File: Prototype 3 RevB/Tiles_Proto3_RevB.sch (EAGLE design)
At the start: 62 parts, among them Q1 DMG3415U-7, U2 MF-DSC-SOT233-MMBT3904, X1 32.768

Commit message: finished placing proto3revB
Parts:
- removed C12: 0.1uF, microbuilder2:CAP_CERAMIC0603_NO
- added C8: (no value), MF_Passives:CAPACITOR_NP_0603
- B+, B-: device wirepad:1,6/0,8 -> wirepad:SMD2
- C1: value 1uF -> (none)
- C10: value 10µF -> (none); device microbuilder2:CAP_CERAMIC0805-NOOUTLINE -> MF_Passives:CAPACITOR_NP_0805
- C11: value 10µF -> (none); device microbuilder2:CAP_CERAMIC0805-NOOUTLINE -> MF_Passives:CAPACITOR_NP_0603
- C2: value 100nf -> (none); device Seeed-OPL-Capacitor:CERAMIC-100NF-50V-10%-X7R(0603) -> MF_Passives:CAPACITOR_NP_0603
- C3: value 10uF -> (none)
- C4: value 22pF -> (none)
- C5: value 10uf -> (none); device Seeed-OPL-Capacitor:CERAMIC-10UF-10V-10%-X5R(0603) -> MF_Passives:CAPACITOR_NP_0603
- C6, C7: value 1uf -> (none); device Seeed-OPL-Capacitor:CERAMIC-1UF-25V-10%-X7R(0603) -> MF_Passives:CAPACITOR_NP_0603
- C9: value 22pF -> (none); device MF_Passives:CAPACITOR_NP_0603 -> MF_Passives:CAPACITOR_NP_0805
- J1: device tiles:CONN_07_SIMSQPAD_BOTTOM -> SparkFun-Connectors:CONN_07
- R1, R2, R3, R4, R7: value 10K 1/10W -> (none); device Seeed-OPL-Resistor:SMD-RES-10K-5%-1/10W(0603) -> MF_Passives:RESISTOR_0603
- R10, R9: value 100K -> (none); device microbuilder2:RESISTOR_0603_NOOUT -> MF_Passives:RESISTOR_0603
- R11: value 10K -> (none); device microbuilder2:RESISTOR_0603_NOOUT -> MF_Passives:RESISTOR_0603
- R12, R13, R14, R15, R6: value 330 -> (none)
- R5: value 100K 1/10W -> (none); device Seeed-OPL-Resistor:SMD-RES-100K-5%-1/10W(0603) -> MF_Passives:RESISTOR_0603
- R8: value 1K 1/10W -> (none); device Seeed-OPL-Resistor:SMD-RES-10K-5%-1/10W(0603) -> MF_Passives:RESISTOR_0603
- TP2, TP3, TP4, TP5, TP6: device microbuilder2:TESTPOINT1.5X2.0MM_NOCREAM -> microbuilder2:TESTPOINTROUND2MM
- renumbered STAT1 to BTL
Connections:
- net 3.3V: now also C2.P$1, C5.P$1, C7.P$1, C9.P$1, R1.P$1, R11.P$2, R2.P$1, R3.P$1, R8.P$1; no longer C10.1, C2.1, C5.1, C7.2, R1.1, R11.1, R2.2, R3.2, R8.2
- net BUZZER: now also R7.P$2; no longer R7.2
- net CAP-INT: now also R3.P$2; no longer R3.1
- net CAP-RES: now also R4.P$1; no longer R4.2
- net DTR: now also C11.P$1; no longer C12.1
- net GND: now also C10.P$2, C2.P$2, C5.P$2, C6.P$2, C7.P$2, C8.P$2, R4.P$2, R5.P$2, R7.P$1, R9.P$2; no longer C10.2, C11.2, C2.2, C5.2, C6.1, C7.1, R4.1, R5.1, R7.1, R9.2
- net N$10: now also R10.P$2; no longer R10.2
- net N$12: now also C8.P$1; no longer C9.P$1
- net N$13: now also C10.P$1, R10.P$1; no longer C11.1, R10.1
- net N$20: now also C11.P$2; no longer C12.2
- net N$3: now also R5.P$1; no longer R5.2
- net N$4: now also R8.P$2; no longer R8.1
- net N$5: now also C6.P$1; no longer C6.2
- net RESET: now also R11.P$1; no longer R11.2
- net SCL: now also R1.P$2; no longer R1.2
- net SDA: now also R2.P$2; no longer R2.1
- net VBUS: now also R9.P$1; no longer R9.1
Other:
- moved on the sheet: C9

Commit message: partial routing
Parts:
- renumbered TP1 to FRST, TP2 to SWDIO, TP3 to SWCLK, TP4 to RST, TP5 to DFU, TP6 to SWO
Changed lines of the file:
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@@
 <part name="U$7" library="microbuilder" deviceset="GND" device=""/>
 <part name="U$8" library="microbuilder" deviceset="GND" device=""/>
-<part name="TP1" library="microbuilder2" deviceset="TESTPOINT" device="1.5X2.0MM_NOCREAM"/>
-<part name="TP2" library="microbuilder2" deviceset="TESTPOINT" device="ROUND2MM"/>
-<part name="TP3" library="microbuilder2" deviceset="TESTPOINT" device="ROUND2MM"/>
-<part name="TP4" library="microbuilder2" deviceset="TESTPOINT" device="ROUND2MM"/>
-<part name="TP5" library="microbuilder2" deviceset="TESTPOINT" device="ROUND2MM"/>
-<part name="TP6" library="microbuilder2" deviceset="TESTPOINT" device="ROUND2MM"/>
+<part name="FRST" library="microbuilder2" deviceset="TESTPOINT" device="1.5X2.0MM_NOCREAM"/>
+<part name="SWDIO" library="microbuilder2" deviceset="TESTPOINT" device="ROUND2MM"/>
+<part name="SWCLK" library="microbuilder2" deviceset="TESTPOINT" device="ROUND2MM"/>
+<part name="RST" library="microbuilder2" deviceset="TESTPOINT" device="ROUND2MM"/>
+<part name="DFU" library="microbuilder2" deviceset="TESTPOINT" device="ROUND2MM"/>
+<part name="SWO" library="microbuilder2" deviceset="TESTPOINT" device="ROUND2MM"/>
 <part name="U$10" library="microbuilder2" deviceset="3.3V" device=""/>
 <part name="U$11" library="microbuilder2" deviceset="VBAT" device=""/>
@@
 <instance part="U$7" gate="G$1" x="-2.54" y="68.58"/>
 <instance part="U$8" gate="G$1" x="60.96" y="78.74" rot="R180"/>
-<instance part="TP1" gate="G$1" x="60.96" y="68.58" rot="R270"/>
-<instance part="TP2" gate="G$1" x="60.96" y="66.04" rot="R270"/>
-<instance part="TP3" gate="G$1" x="60.96" y="63.5" rot="R270"/>
-<instance part="TP4" gate="G$1" x="60.96" y="60.96" rot="R270"/>
-<instance part="TP5" gate="G$1" x="60.96" y="58.42" rot="R270"/>
-<instance part="TP6" gate="G$1" x="60.96" y="53.34" rot="R270"/>
+<instance part="FRST" gate="G$1" x="60.96" y="68.58" rot="R270"/>
+<instance part="SWDIO" gate="G$1" x="60.96" y="66.04" rot="R270"/>
+<instance part="SWCLK" gate="G$1" x="60.96" y="63.5" rot="R270"/>
+<instance part="RST" gate="G$1" x="60.96" y="60.96" rot="R270"/>
+<instance part="DFU" gate="G$1" x="60.96" y="58.42" rot="R270"/>
+<instance part="SWO" gate="G$1" x="60.96" y="53.34" rot="R270"/>
 <instance part="U$10" gate="G$1" x="43.18" y="162.56"/>
 <instance part="U$11" gate="G$1" x="2.54" y="162.56"/>
@@
 <segment>
 <pinref part="U1" gate="G$1" pin="P0.21/RESET"/>
-<pinref part="TP4" gate="G$1" pin="P$1"/>
+<pinref part="RST" gate="G$1" pin="P$1"/>
 <wire x1="45.72" y1="60.96" x2="60.96" y2="60.96" width="0.1524" layer="91"/>
 <label x="48.26" y="60.96" size="1.778" layer="95"/>
@@
 <segment>
 <pinref part="U1" gate="G$1" pin="P0.22"/>
-<pinref part="TP1" gate="G$1" pin="P$1"/>
+<pinref part="FRST" gate="G$1" pin="P$1"/>
 <wire x1="45.72" y1="68.58" x2="60.96" y2="68.58" width="0.1524" layer="91"/>
 <label x="48.26" y="68.58" size="1.778" layer="95"/>
@@
 <segment>
 <pinref part="U1" gate="G$1" pin="SWDIO"/>
-<pinref part="TP2" gate="G$1" pin="P$1"/>
+<pinref part="SWDIO" gate="G$1" pin="P$1"/>
 <wire x1="45.72" y1="66.04" x2="60.96" y2="66.04" width="0.1524" layer="91"/>
 <label x="48.26" y="66.04" size="1.778" layer="95"/>
@@
 <segment>
 <pinref part="U1" gate="G$1" pin="SWDCLK"/>
-<pinref part="TP3" gate="G$1" pin="P$1"/>
+<pinref part="SWCLK" gate="G$1" pin="P$1"/>
 <wire x1="45.72" y1="63.5" x2="60.96" y2="63.5" width="0.1524" layer="91"/>
 <label x="48.26" y="63.5" size="1.778" layer="95"/>
@@
 <segment>
 <pinref part="U1" gate="G$1" pin="P0.20"/>
-<pinref part="TP5" gate="G$1" pin="P$1"/>
+<pinref part="DFU" gate="G$1" pin="P$1"/>
 <wire x1="45.72" y1="58.42" x2="60.96" y2="58.42" width="0.1524" layer="91"/>
 <label x="48.26" y="58.42" size="1.778" layer="95"/>
@@
 <segment>
 <pinref part="U1" gate="G$1" pin="P0.18/SWO"/>
-<pinref part="TP6" gate="G$1" pin="P$1"/>
+<pinref part="SWO" gate="G$1" pin="P$1"/>
 <wire x1="45.72" y1="53.34" x2="60.96" y2="53.34" width="0.1524" layer="91"/>
 <label x="48.26" y="53.34" size="1.778" layer="95"/>

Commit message: ready for prod
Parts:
- removed IMU: ADXL345BCCZ-RL, Seeed-OPL-sensor:MOTION/POSITION-ADXL345BCCZ-RL(14P-5.0X3.0MM)
- added EN: (no value), SparkFun-Connectors:CONN_021X02_NO_SILK
- added T2: MF-DSC-SOT233-MMBT3904, MF_Discrete_Semiconductor:NPN_BJTMMBT3904_SOT-23-3
- U1: value (none) -> MDBT42Q
- U2: value MF-DSC-SOT233-MMBT3904 -> AP2112; device MF_Discrete_Semiconductor:NPN_BJTMMBT3904_SOT-23-3 -> microbuilder2:VREG_SOT23-5
- U3: value (none) -> ADXL345; device microbuilder2:VREG_SOT23-5 -> Seeed-OPL-sensor:MOTION/POSITION-ADXL345BCCZ-RL(14P-5.0X3.0MM)
- U4: value (none) -> CAP1188
- renumbered CAP to U4, HAPTIC to U5
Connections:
- removed net N$10: R10.P$2, U3.EN
- new net EN: EN.1, R10.P$2, U2.EN
- net 3.3V: now also U2.OUT, U3.!CS, U3.VDDI/O, U3.VS; no longer IMU.!CS, IMU.VDDI/O, IMU.VS, U3.OUT
- net BUZZER: now also T2.BASE; no longer U2.BASE
- net GND: now also EN.2, T2.EMITTER, U2.GND, U3.GND@1, U3.GND@2, U3.GND@3; no longer IMU.GND@1, IMU.GND@2, IMU.GND@3, U2.EMITTER, U3.GND
- net IMU-INT: now also U3.INT1; no longer IMU.INT1
- net N$13: now also U2.IN; no longer U3.IN
- net N$4: now also T2.COLLECTOR; no longer U2.COLLECTOR
- net SCL: now also U3.SCL/SCLK; no longer IMU.SCL/SCLK
- net SDA: now also U3.SDA/SDI/SDIO; no longer IMU.SDA/SDI/SDIO

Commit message: values back in sch
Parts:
- C1, C6, C7: value (none) -> 1uF
- C10, C5, C9: value (none) -> 10uF
- C11: value (none) -> 0.1uF
- C2: value (none) -> 100nF
- C4, C8: value (none) -> 22pF
- L1: value (none) -> 10uH
- R1, R11, R2, R3, R4, R7: value (none) -> 10K
- R10, R5, R9: value (none) -> 100K
- R12: value (none) -> 27
- R13, R14: value (none) -> 22
- R15, R6: value (none) -> 330
- R8: value (none) -> 1K
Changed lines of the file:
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@@
 <part name="SW" library="MF_Switches" deviceset="TACT" device="_4.2MM" value="MF-SW-TACT-4.2MM"/>
 <part name="STAT" library="MF_LEDs" deviceset="LED_SINGLE" device="-0603-RED" value="MF-LED-0603-RED"/>
-<part name="R6" library="MF_Passives" deviceset="RESISTOR" device="_0603"/>
+<part name="R6" library="MF_Passives" deviceset="RESISTOR" device="_0603" value="330"/>
 <part name="U$21" library="microbuilder" deviceset="GND" device=""/>
 <part name="U$25" library="microbuilder" deviceset="GND" device=""/>
@@
 <part name="U3" library="Seeed-OPL-sensor" deviceset="MOTION/POSITION-ADXL345BCCZ-RL(14P-5.0X3.0MM)" device="" value="ADXL345"/>
 <part name="U1" library="microbuilder2" deviceset="NRF52832_MODULE_MDBT42" device="" value="MDBT42Q"/>
-<part name="C1" library="MF_Passives" deviceset="CAPACITOR_NP" device="_0603"/>
+<part name="C1" library="MF_Passives" deviceset="CAPACITOR_NP" device="_0603" value="1uF"/>
 <part name="C3" library="MF_Passives" deviceset="CAPACITOR_NP" device="_0603"/>
-<part name="C4" library="MF_Passives" deviceset="CAPACITOR_NP" device="_0603"/>
-<part name="C8" library="MF_Passives" deviceset="CAPACITOR_NP" device="_0603"/>
-<part name="L1" library="MF_Passives" deviceset="INDUCTOR" device="_0603"/>
+<part name="C4" library="MF_Passives" deviceset="CAPACITOR_NP" device="_0603" value="22pF"/>
+<part name="C8" library="MF_Passives" deviceset="CAPACITOR_NP" device="_0603" value="22pF"/>
+<part name="L1" library="MF_Passives" deviceset="INDUCTOR" device="_0603" value="10uH"/>
 <part name="U$1" library="microbuilder2" deviceset="3.3V" device=""/>
 <part name="U$2" library="microbuilder" deviceset="GND" device=""/>
@@
 <part name="U$35" library="microbuilder" deviceset="GND" device=""/>
 <part name="P+2" library="microbuilder2" deviceset="3.3V" device=""/>
-<part name="R12" library="MF_Passives" deviceset="RESISTOR" device="_0603"/>
-<part name="R13" library="MF_Passives" deviceset="RESISTOR" device="_0603"/>
-<part name="R14" library="MF_Passives" deviceset="RESISTOR" device="_0603"/>
+<part name="R12" library="MF_Passives" deviceset="RESISTOR" device="_0603" value="27"/>
+<part name="R13" library="MF_Passives" deviceset="RESISTOR" device="_0603" value="22"/>
+<part name="R14" library="MF_Passives" deviceset="RESISTOR" device="_0603" value="22"/>
 <part name="D3" library="MF_LEDs" deviceset="LED_RGB_CA" device="_PLCC4" value="MF-LED-3228-RGB"/>
 <part name="BTL" library="MF_LEDs" deviceset="LED_SINGLE" device="-0603-RED" value="MF-LED-0603-RED"/>
-<part name="R15" library="MF_Passives" deviceset="RESISTOR" device="_0603"/>
+<part name="R15" library="MF_Passives" deviceset="RESISTOR" device="_0603" value="330"/>
 <part name="U$18" library="microbuilder" deviceset="GND" device=""/>
-<part name="R9" library="MF_Passives" deviceset="RESISTOR" device="_0603"/>
-<part name="R10" library="MF_Passives" deviceset="RESISTOR" device="_0603"/>
-<part name="R11" library="MF_Passives" deviceset="RESISTOR" device="_0603"/>
-<part name="R1" library="MF_Passives" deviceset="RESISTOR" device="_0603"/>
-<part name="R2" library="MF_Passives" deviceset="RESISTOR" device="_0603"/>
-<part name="R3" library="MF_Passives" deviceset="RESISTOR" device="_0603"/>
-<part name="R4" library="MF_Passives" deviceset="RESISTOR" device="_0603"/>
-<part name="R5" library="MF_Passives" deviceset="RESISTOR" device="_0603"/>
-<part name="R7" library="MF_Passives" deviceset="RESISTOR" device="_0603"/>
-<part name="R8" library="MF_Passives" deviceset="RESISTOR" device="_0603"/>
-<part name="C2" library="MF_Passives" deviceset="CAPACITOR_NP" device="_0603"/>
-<part name="C5" library="MF_Passives" deviceset="CAPACITOR_NP" device="_0603"/>
-<part name="C6" library="MF_Passives" deviceset="CAPACITOR_NP" device="_0603"/>
-<part name="C7" library="MF_Passives" deviceset="CAPACITOR_NP" device="_0603"/>
-<part name="C9" library="MF_Passives" deviceset="CAPACITOR_NP" device="_0805"/>
-<part name="C10" library="MF_Passives" deviceset="CAPACITOR_NP" device="_0805"/>
-<part name="C11" library="MF_Passives" deviceset="CAPACITOR_NP" device="_0603"/>
+<part name="R9" library="MF_Passives" deviceset="RESISTOR" device="_0603" value="100K"/>
+<part name="R10" library="MF_Passives" deviceset="RESISTOR" device="_0603" value="100K"/>
+<part name="R11" library="MF_Passives" deviceset="RESISTOR" device="_0603" value="10K"/>
+<part name="R1" library="MF_Passives" deviceset="RESISTOR" device="_0603" value="10K"/>
+<part name="R2" library="MF_Passives" deviceset="RESISTOR" device="_0603" value="10K"/>
+<part name="R3" library="MF_Passives" deviceset="RESISTOR" device="_0603" value="10K"/>
+<part name="R4" library="MF_Passives" deviceset="RESISTOR" device="_0603" value="10K"/>
+<part name="R5" library="MF_Passives" deviceset="RESISTOR" device="_0603" value="100K"/>
+<part name="R7" library="MF_Passives" deviceset="RESISTOR" device="_0603" value="10K"/>
+<part name="R8" library="MF_Passives" deviceset="RESISTOR" device="_0603" value="1K"/>
+<part name="C2" library="MF_Passives" deviceset="CAPACITOR_NP" device="_0603" value="100nF"/>
+<part name="C5" library="MF_Passives" deviceset="CAPACITOR_NP" device="_0603" value="10uF"/>
+<part name="C6" library="MF_Passives" deviceset="CAPACITOR_NP" device="_0603" value="1uF"/>
+<part name="C7" library="MF_Passives" deviceset="CAPACITOR_NP" device="_0603" value="1uF"/>
+<part name="C9" library="MF_Passives" deviceset="CAPACITOR_NP" device="_0805" value="10uF"/>
+<part name="C10" library="MF_Passives" deviceset="CAPACITOR_NP" device="_0805" value="10uF"/>
+<part name="C11" library="MF_Passives" deviceset="CAPACITOR_NP" device="_0603" value="0.1uF"/>
 <part name="B+" library="wirepad" deviceset="SMD2" device=""/>
 <part name="B-" library="wirepad" deviceset="SMD2" device=""/>

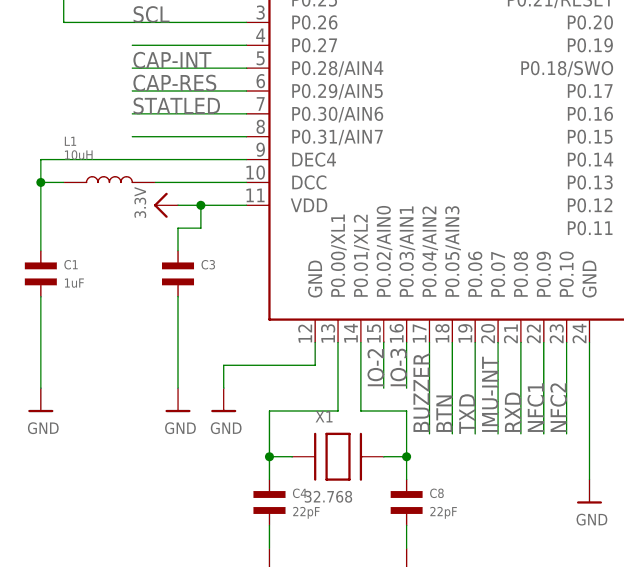
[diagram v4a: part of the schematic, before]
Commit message: re-added part values
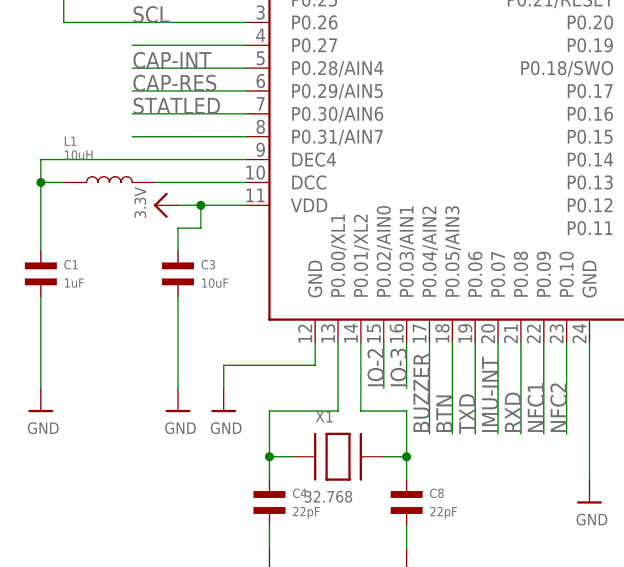
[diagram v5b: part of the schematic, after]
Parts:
- C3: value (none) -> 10uF
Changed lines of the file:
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@@
 <part name="U1" library="microbuilder2" deviceset="NRF52832_MODULE_MDBT42" device="" value="MDBT42Q"/>
 <part name="C1" library="MF_Passives" deviceset="CAPACITOR_NP" device="_0603" value="1uF"/>
-<part name="C3" library="MF_Passives" deviceset="CAPACITOR_NP" device="_0603"/>
+<part name="C3" library="MF_Passives" deviceset="CAPACITOR_NP" device="_0603" value="10uF"/>
 <part name="C4" library="MF_Passives" deviceset="CAPACITOR_NP" device="_0603" value="22pF"/>
 <part name="C8" library="MF_Passives" deviceset="CAPACITOR_NP" device="_0603" value="22pF"/>
@@
 </sheet>
 </sheets>
+<errors>
+</errors>
 </schematic>
 </drawing>

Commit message: ready for prod
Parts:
- BTL: value MF-LED-0603-RED -> RED
- BUZZER: HOUSEPART (none) -> no; MPN (none) -> 490-CMT-4023S-SMT-TR; POPULATE (none) -> 1
- C1, C6, C7: HOUSEPART (none) -> YES; MPN (none) -> MF-CAP-0603-1uF
- C10, C9: device MF_Passives:CAPACITOR_NP_0805 -> MF_Passives:CAPACITOR_NP_1206; HOUSEPART (none) -> YES; MPN (none) -> MF-CAP-1206-10uF
- C11: HOUSEPART (none) -> YES; MPN (none) -> MF-CAP-0603-0.1uF
- C2: value 100nF -> 0.1uF; HOUSEPART (none) -> YES; MPN (none) -> MF-CAP-0603-0.1uF
- C3, C5: device MF_Passives:CAPACITOR_NP_0603 -> MF_Passives:CAPACITOR_NP_1206; HOUSEPART (none) -> YES; MPN (none) -> MF-CAP-1206-10uF
- C4, C8: HOUSEPART (none) -> YES; MPN (none) -> MF-CAP-0603-22pF
- CAP-A, CAP-B, DFU, EN, FRST, GPIO, I2C, IO-2, IO-3, RESW, RST, SWCLK, SWDIO, SWO, TOUCH: POPULATE (none) -> 0
- D1: HOUSEPART (none) -> NO; MPN (none) -> MBR120LSFT1G; POPULATE (none) -> 1
- D2: device microbuilder2:DIODESOD-323 -> MF_Discrete_Semiconductor:DIODES_1N4148_SOD-123
- D3: value MF-LED-3228-RGB -> RGBLED
- L1: device MF_Passives:INDUCTOR_0603 -> MF_Passives:INDUCTOR_1210; HOUSEPART (none) -> YES; MPN (none) -> MF-IND-1210-10uH; POPULATE (none) -> 1
- Q1: HOUSEPART (none) -> YES; MPN (none) -> MF-DSC-SOT233-BSS84; POPULATE (none) -> 1
- R1, R11, R2, R3, R4, R7: HOUSEPART (none) -> YES; MPN (none) -> MF-RES-0603-10K
- R10, R5, R9: HOUSEPART (none) -> YES; MPN (none) -> MF-RES-0603-100K
- R12: HOUSEPART (none) -> YES; MPN (none) -> MF-RES-0603-27
- R13, R14: HOUSEPART (none) -> YES; MPN (none) -> MF-RES-0603-22
- R15, R6: HOUSEPART (none) -> YES; MPN (none) -> MF-RES-0603-330
- R8: HOUSEPART (none) -> YES; MPN (none) -> MF-RES-0603-1K
- STAT: value MF-LED-0603-RED -> WHITE; HOUSEPART (none) -> NO; MPN (none) -> LNJ037X8ARA
- SW: value MF-SW-TACT-4.2MM -> SW
- T2: value MF-DSC-SOT233-MMBT3904 -> MMBT3904
- U1: HOUSEPART (none) -> NO; MPN (none) -> 317030213; POPULATE (none) -> 1
- U2: HOUSEPART (none) -> NO; MPN (none) -> AP2112K-3.3TRG1; POPULATE (none) -> 1
- U3: HOUSEPART (none) -> no; POPULATE (none) -> 1
- U4: HOUSEPART (none) -> NO; MPN (none) -> CAP1188-1-CP-TR; POPULATE (none) -> 1
- U5: HOUSEPART (none) -> NO; MPN (none) -> DRV2605LDGST; POPULATE (none) -> 1
- X1: HOUSEPART (none) -> no; MPN (none) -> ABS07-120-32.768KHZ-T; POPULATE (none) -> 1
- renumbered SW1 to RESW
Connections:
- net 3.3V: now also D2.CATHODE; no longer D2.C
- net RESET: now also D2.ANODE; no longer D2.A
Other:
- moved on the sheet: D3, R12, R13, R14
